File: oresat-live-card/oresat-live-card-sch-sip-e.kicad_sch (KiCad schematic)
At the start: 1 part, among them U7 OSD3358-512M-BSM

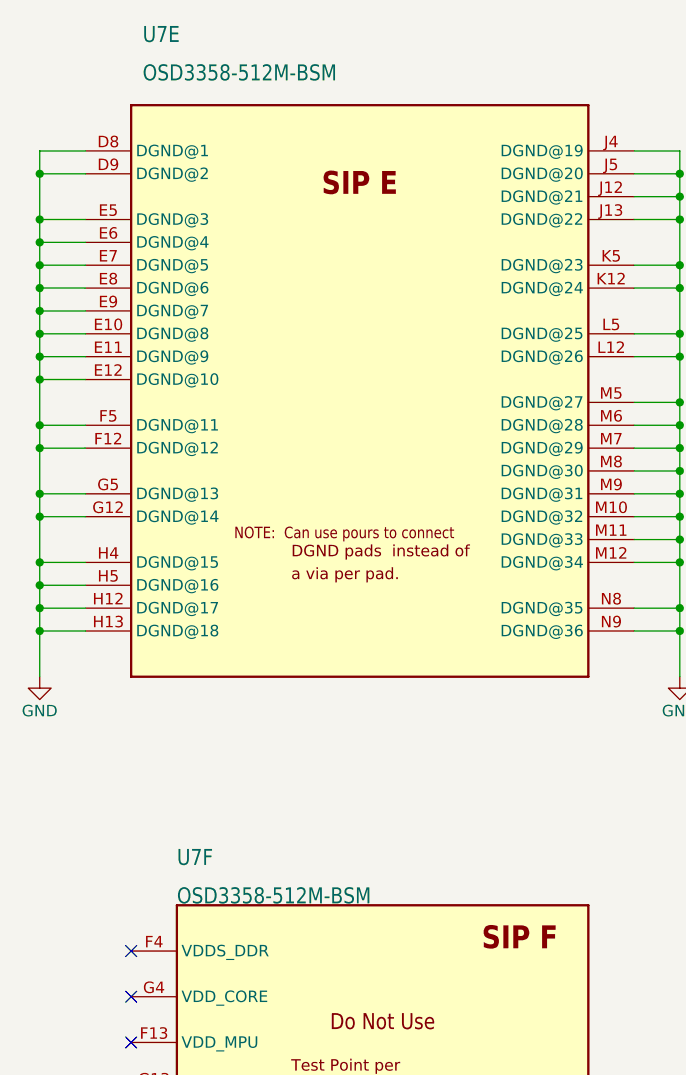
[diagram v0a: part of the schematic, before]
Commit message: BOM changes
Updated components outside of RF path to on hand parts.
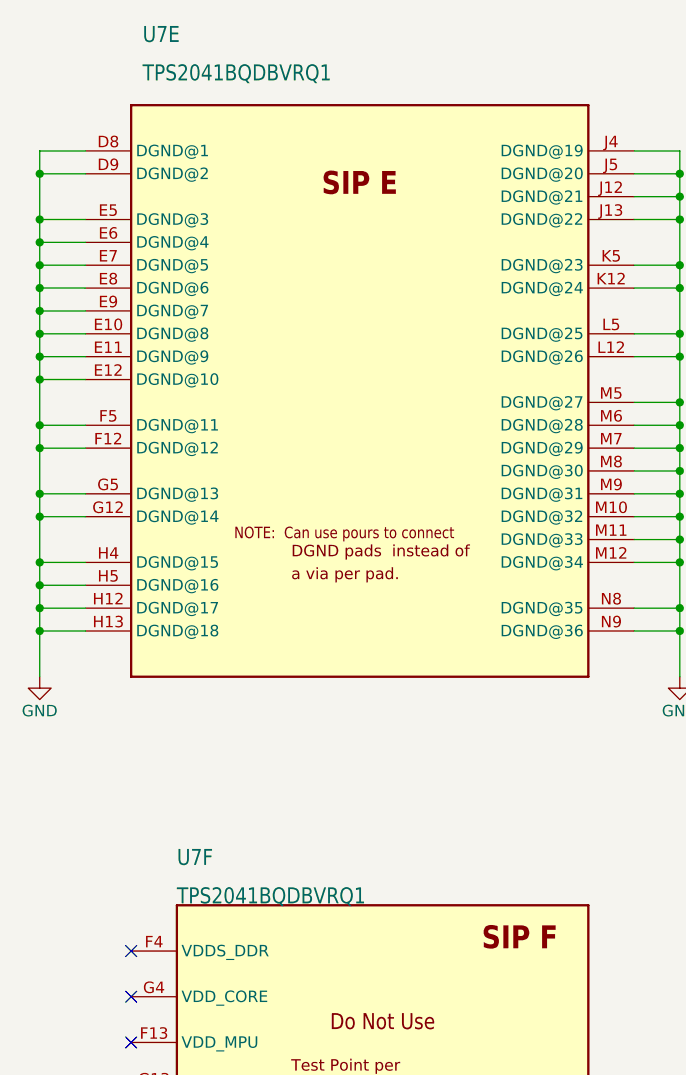
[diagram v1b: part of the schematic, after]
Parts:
- U7: value OSD3358-512M-BSM -> TPS2041BQDBVRQ1; footprint oresat-ics:U-Octavo-OSD335X-BGA-256 -> oresat-live-card:DBV5; DPN 1676-1002-ND -> 296-25159-1-ND; MFR Octavo Systems -> Texas Instruments; MPN OSD3358-512M-BSM -> TPS2041BQDBVRQ1
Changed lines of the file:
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@@
 			)
 		)
-		(property "Value" "OSD3358-512M-BSM"
+		(property "Value" "TPS2041BQDBVRQ1"
 			(at 162.56 52.07 0)
 			(show_name no)
@@
 			)
 		)
-		(property "Footprint" "oresat-ics:U-Octavo-OSD335X-BGA-256"
+		(property "Footprint" "oresat-live-card:DBV5"
 			(at 186.69 -22.86 0)
 			(hide yes)
@@
 			)
 		)
-		(property "Datasheet" ""
+		(property "Datasheet" "https://www.ti.com/lit/ds/symlink/tps2041b-q1.pdf?HQS=dis-dk-null-digikeymode-dsf-pf-null-wwe&ts=1651525711603&ref_url=https%253A%252F%252Fwww.ti.com%252Fgeneral%252Fdocs%252Fsuppproductinfo.tsp%253FdistId%253D10%2526gotoUrl%253Dhttps%253A%252F%252Fwww.ti.com%252Flit%252Fgpn%252Ftps2041b-q1"
 			(at 186.69 85.09 0)
 			(hide yes)
@@
 			)
 		)
-		(property "Description" "OSD335x Embedded Module 1GHz 512MB"
+		(property "Description" "Power Switch/Driver 1:1 N-Channel 500mA"
 			(at 186.69 85.09 0)
 			(hide yes)
@@
 			)
 		)
-		(property "MPN" "OSD3358-512M-BSM"
+		(property "MPN" "TPS2041BQDBVRQ1"
 			(at 186.69 85.09 0)
 			(hide yes)
@@
 			)
 		)
-		(property "DPN" "1676-1002-ND "
+		(property "DPN" "296-25159-1-ND "
 			(at 186.69 85.09 0)
 			(hide yes)
@@
 			)
 		)
-		(property "MFR" "Octavo Systems "
+		(property "MFR" "Texas Instruments "
 			(at 186.69 85.09 0)
 			(hide yes)
@@
 			)
 		)
-		(property "Value" "OSD3358-512M-BSM"
+		(property "Value" "TPS2041BQDBVRQ1"
 			(at 166.37 143.51 0)
 			(show_name no)
@@
 			)
 		)
-		(property "Footprint" "oresat-ics:U-Octavo-OSD335X-BGA-256"
+		(property "Footprint" "oresat-live-card:DBV5"
 			(at 189.23 60.96 0)
 			(hide yes)
@@
 			)
 		)
-		(property "Datasheet" ""
+		(property "Datasheet" "https://www.ti.com/lit/ds/symlink/tps2041b-q1.pdf?HQS=dis-dk-null-digikeymode-dsf-pf-null-wwe&ts=1651525711603&ref_url=https%253A%252F%252Fwww.ti.com%252Fgeneral%252Fdocs%252Fsuppproductinfo.tsp%253FdistId%253D10%2526gotoUrl%253Dhttps%253A%252F%252Fwww.ti.com%252Flit%252Fgpn%252Ftps2041b-q1"
 			(at 189.23 168.91 0)
 			(hide yes)
@@
 			)
 		)
-		(property "Description" "OSD335x Embedded Module 1GHz 512MB"
+		(property "Description" "Power Switch/Driver 1:1 N-Channel 500mA"
 			(at 189.23 168.91 0)
 			(hide yes)
@@
 			)
 		)
-		(property "MPN" "OSD3358-512M-BSM"
+		(property "MPN" "TPS2041BQDBVRQ1"
 			(at 189.23 168.91 0)
 			(hide yes)
@@
 			)
 		)
-		(property "DPN" "1676-1002-ND "
+		(property "DPN" "296-25159-1-ND "
 			(at 189.23 168.91 0)
 			(hide yes)
@@
 			)
 		)
-		(property "MFR" "Octavo Systems "
+		(property "MFR" "Texas Instruments "
 			(at 189.23 168.91 0)
 			(hide yes)

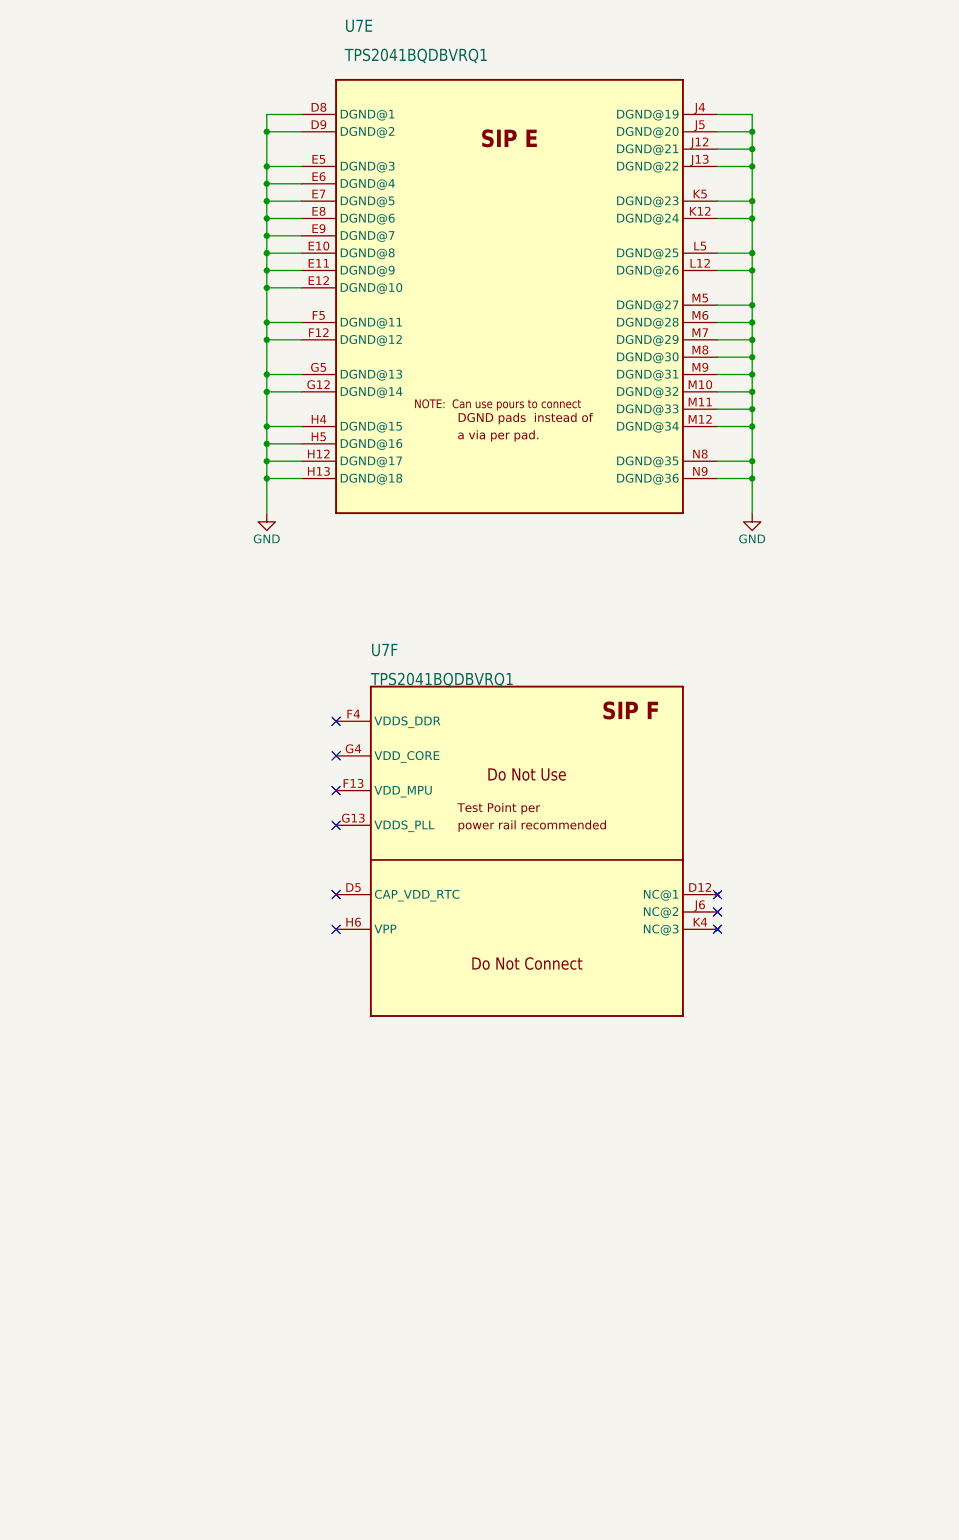
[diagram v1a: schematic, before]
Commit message: Cleanup of main sheet, no changes to functionality
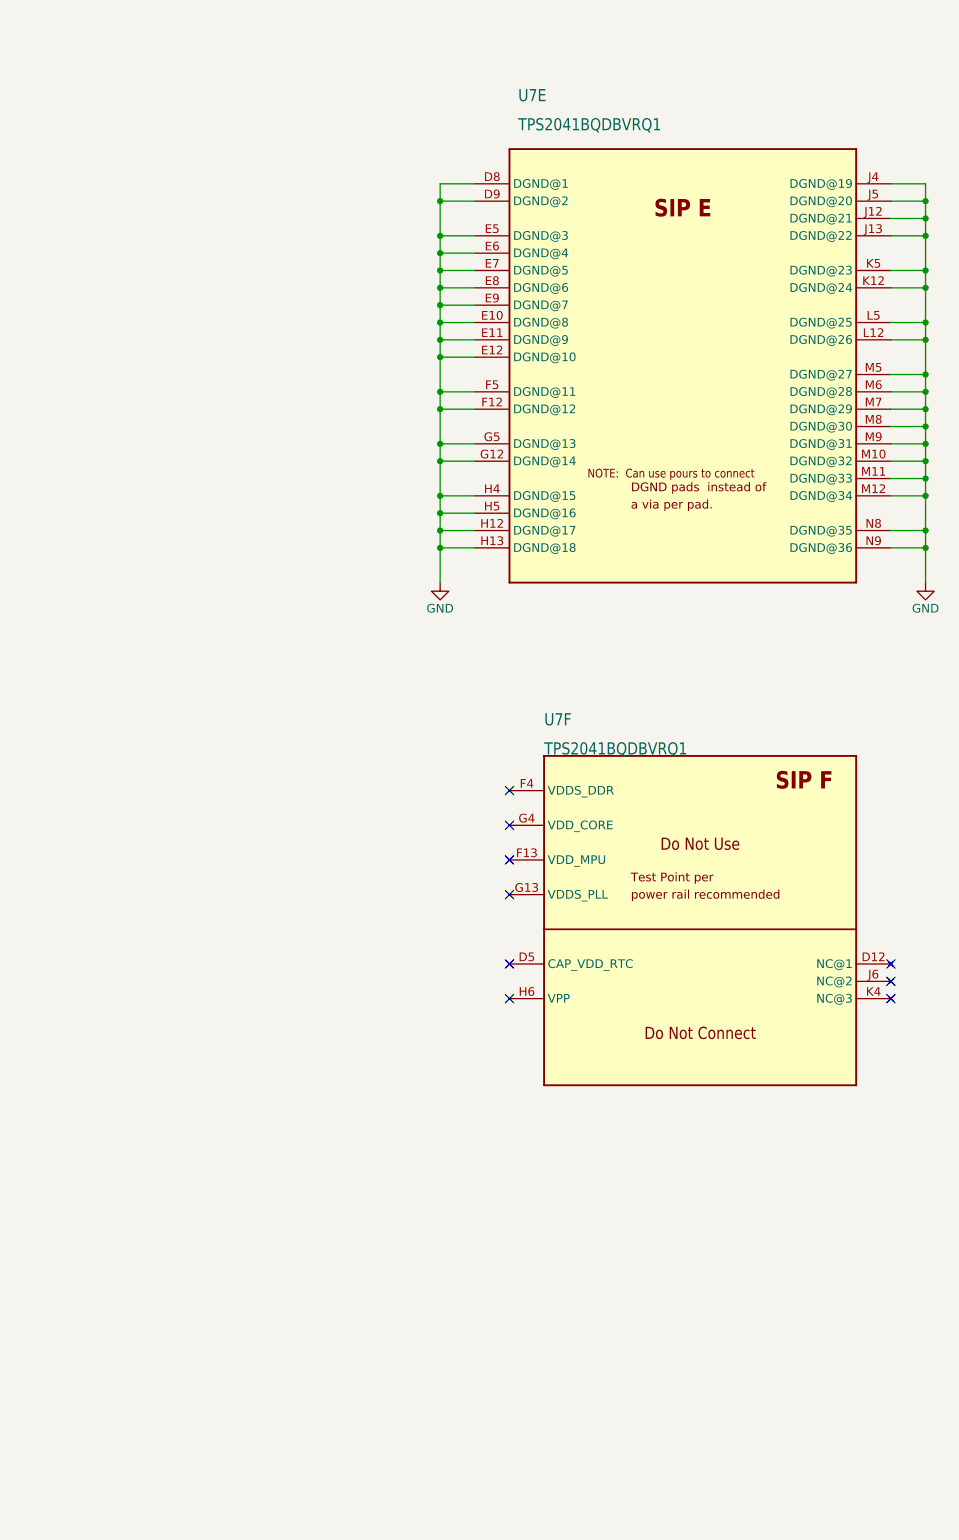
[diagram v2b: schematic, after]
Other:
- moved on the sheet: U7E, U7F

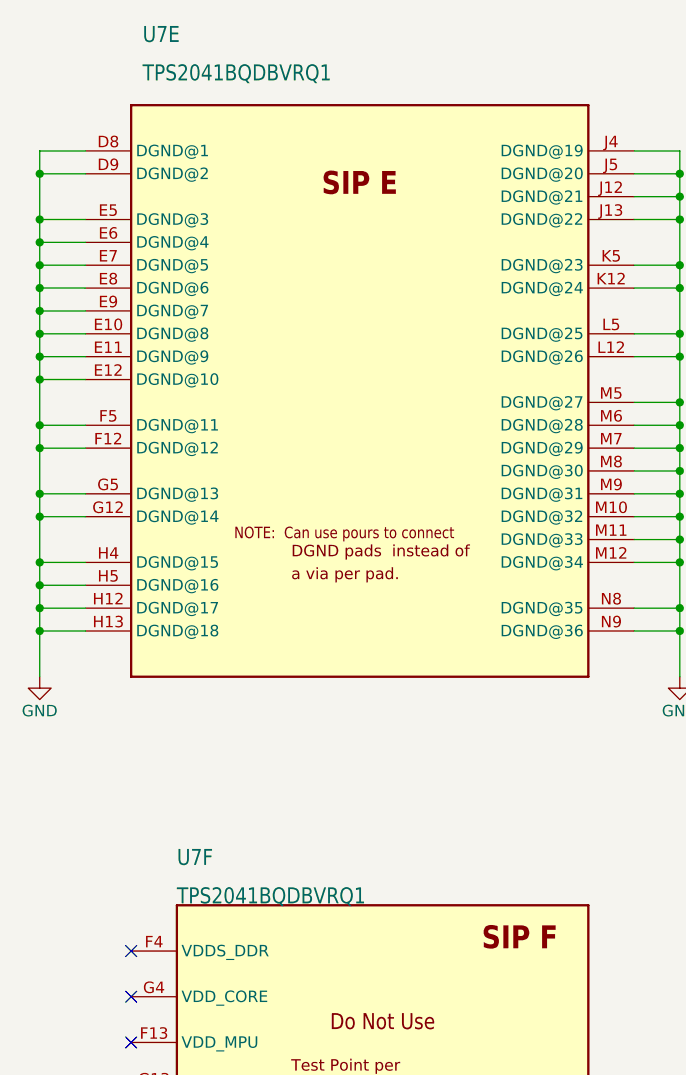
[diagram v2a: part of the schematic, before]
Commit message: BOM changed to match older version
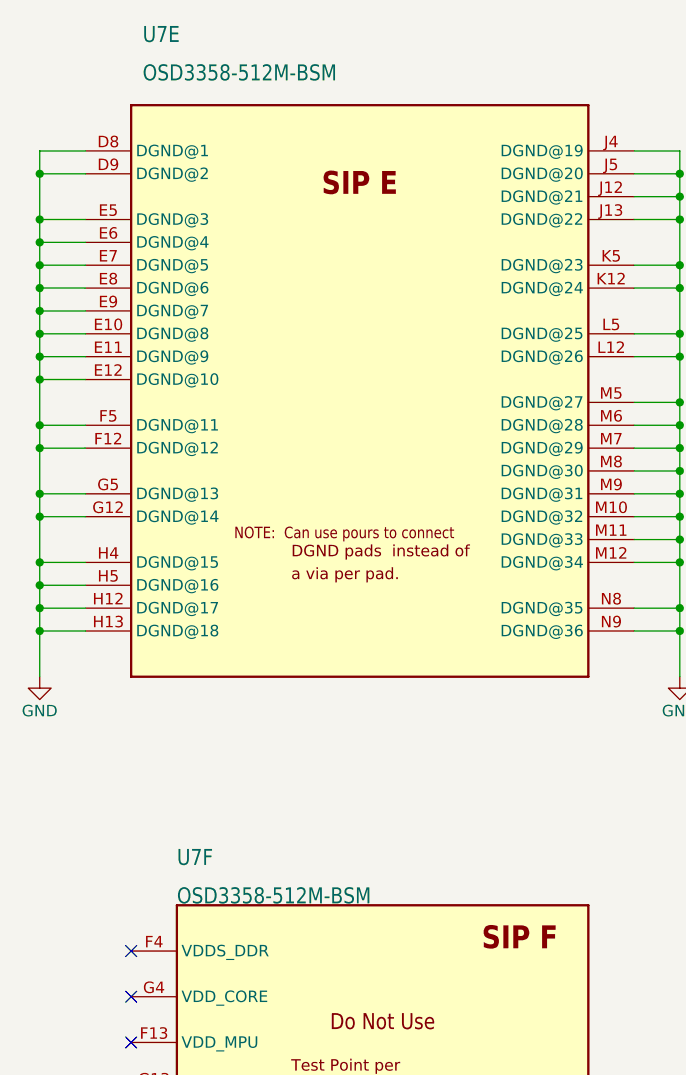
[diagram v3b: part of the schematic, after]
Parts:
- U7: value TPS2041BQDBVRQ1 -> OSD3358-512M-BSM; footprint oresat-live-card:DBV5 -> oresat-ics:U-Octavo-OSD335X-BGA-256; DPN 296-25159-1-ND -> 1676-1002-ND; MFR Texas Instruments -> Octavo Systems; MPN TPS2041BQDBVRQ1 -> OSD3358-512M-BSM
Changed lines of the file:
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@@
 			)
 		)
-		(property "Value" "TPS2041BQDBVRQ1"
+		(property "Value" "OSD3358-512M-BSM"
 			(at 187.96 62.23 0)
 			(show_name no)
@@
 			)
 		)
-		(property "Footprint" "oresat-live-card:DBV5"
+		(property "Footprint" "oresat-ics:U-Octavo-OSD335X-BGA-256"
 			(at 212.09 -12.7 0)
 			(hide yes)
@@
 			)
 		)
-		(property "Description" "Power Switch/Driver 1:1 N-Channel 500mA"
+		(property "Description" "OSD335x Embedded Module 1GHz 512MB"
 			(at 212.09 95.25 0)
 			(hide yes)
@@
 			)
 		)
-		(property "MPN" "TPS2041BQDBVRQ1"
+		(property "MPN" "OSD3358-512M-BSM"
 			(at 212.09 95.25 0)
 			(hide yes)
@@
 			)
 		)
-		(property "DPN" "296-25159-1-ND "
+		(property "DPN" "1676-1002-ND"
 			(at 212.09 95.25 0)
 			(hide yes)
@@
 			)
 		)
-		(property "MFR" "Texas Instruments "
+		(property "MFR" "Octavo Systems"
 			(at 212.09 95.25 0)
 			(hide yes)
@@
 			)
 		)
-		(property "Value" "TPS2041BQDBVRQ1"
+		(property "Value" "OSD3358-512M-BSM"
 			(at 191.77 153.67 0)
 			(show_name no)
@@
 			)
 		)
-		(property "Footprint" "oresat-live-card:DBV5"
+		(property "Footprint" "oresat-ics:U-Octavo-OSD335X-BGA-256"
 			(at 214.63 71.12 0)
 			(hide yes)
@@
 			)
 		)
-		(property "Description" "Power Switch/Driver 1:1 N-Channel 500mA"
+		(property "Description" "OSD335x Embedded Module 1GHz 512MB"
 			(at 214.63 179.07 0)
 			(hide yes)
@@
 			)
 		)
-		(property "MPN" "TPS2041BQDBVRQ1"
+		(property "MPN" "OSD3358-512M-BSM"
 			(at 214.63 179.07 0)
 			(hide yes)
@@
 			)
 		)
-		(property "DPN" "296-25159-1-ND "
+		(property "DPN" "1676-1002-ND"
 			(at 214.63 179.07 0)
 			(hide yes)
@@
 			)
 		)
-		(property "MFR" "Texas Instruments "
+		(property "MFR" "Octavo Systems"
 			(at 214.63 179.07 0)
 			(hide yes)

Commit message: mostly just polish after BOM fixes
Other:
- note added: "All resistors 0603 +/- 1% unless marked and AEQ certified unless otherwise marked. All caps are 0603 10% X5R or better and Vw >= 25 V and AEQ certified unless otherwise marked."
- moved on the sheet: U7F
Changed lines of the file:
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@@
 		(rev "2.1")
 	)
+	(text "All resistors 0603 +/- 1% unless marked and AEQ certified unless otherwise marked.\nAll caps are 0603 10% X5R or better and Vw >= 25 V and AEQ certified unless otherwise marked."
+		(exclude_from_sim no)
+		(at 114.046 265.938 0)
+		(effects
+			(font
+				(size 1.778 1.5113)
+			)
+			(justify left bottom)
+		)
+	)
 	(junction
 		(at 247.65 100.33)
@@
 	)
 	(no_connect
-		(at 186.69 163.83)
+		(at 185.42 163.83)
 	)
 	(no_connect
-		(at 242.57 189.23)
+		(at 241.3 189.23)
 	)
 	(no_connect
-		(at 242.57 186.69)
+		(at 241.3 186.69)
 	)
 	(no_connect
-		(at 186.69 189.23)
+		(at 185.42 189.23)
 	)
 	(no_connect
-		(at 242.57 184.15)
+		(at 241.3 184.15)
 	)
 	(no_connect
-		(at 186.69 168.91)
+		(at 185.42 168.91)
 	)
 	(no_connect
-		(at 186.69 184.15)
+		(at 185.42 184.15)
 	)
 	(no_connect
-		(at 186.69 173.99)
+		(at 185.42 173.99)
 	)
 	(no_connect
-		(at 186.69 158.75)
+		(at 185.42 158.75)
 	)
 	(wire
@@
 			(effects
 				(font
-					(size 1.778 1.5113)
+					(size 1.27 1.27)
 				)
 				(justify left top)
@@
 			(effects
 				(font
-					(size 1.778 1.5113)
+					(size 1.27 1.27)
 				)
 				(justify left bottom)
@@
 	(symbol
 		(lib_id "oresat-ics:OSD3358-512M-BSM")
-		(at 214.63 179.07 0)
+		(at 213.36 179.07 0)
 		(unit 6)
 		(body_style 1)
@@
 		(dnp no)
 		(property "Reference" "U7"
-			(at 191.77 147.32 0)
-			(show_name no)
-			(do_not_autoplace no)
-			(effects
-				(font
-					(size 1.778 1.5113)
+			(at 190.5 147.32 0)
+			(show_name no)
+			(do_not_autoplace no)
+			(effects
+				(font
+					(size 1.27 1.27)
 				)
 				(justify left top)
@@
 		)
 		(property "Value" "OSD3358-512M-BSM"
-			(at 191.77 153.67 0)
-			(show_name no)
-			(do_not_autoplace no)
-			(effects
-				(font
-					(size 1.778 1.5113)
+			(at 190.5 153.67 0)
+			(show_name no)
+			(do_not_autoplace no)
+			(effects
+				(font
+					(size 1.27 1.27)
 				)
 				(justify left bottom)
@@
 		)
 		(property "Footprint" "oresat-ics:U-Octavo-OSD335X-BGA-256"
-			(at 214.63 71.12 0)
+			(at 213.36 71.12 0)
 			(hide yes)
 			(show_name no)
@@
 		)
 		(property "Datasheet" "https://www.ti.com/lit/ds/symlink/tps2041b-q1.pdf?HQS=dis-dk-null-digikeymode-dsf-pf-null-wwe&ts=1651525711603&ref_url=https%253A%252F%252Fwww.ti.com%252Fgeneral%252Fdocs%252Fsuppproductinfo.tsp%253FdistId%253D10%2526gotoUrl%253Dhttps%253A%252F%252Fwww.ti.com%252Flit%252Fgpn%252Ftps2041b-q1"
-			(at 214.63 179.07 0)
+			(at 213.36 179.07 0)
 			(hide yes)
 			(show_name no)
@@
 		)
 		(property "Description" "OSD335x Embedded Module 1GHz 512MB"
-			(at 214.63 179.07 0)
+			(at 213.36 179.07 0)
 			(hide yes)
 			(show_name no)
@@
 		)
 		(property "MPN" "OSD3358-512M-BSM"
-			(at 214.63 179.07 0)
+			(at 213.36 179.07 0)
 			(hide yes)
 			(show_name no)
@@
 		)
 		(property "DPN" "1676-1002-ND"
-			(at 214.63 179.07 0)
+			(at 213.36 179.07 0)
 			(hide yes)
 			(show_name no)
@@
 		)
 		(property "MFR" "Octavo Systems"
-			(at 214.63 179.07 0)
+			(at 213.36 179.07 0)
 			(hide yes)
 			(show_name no)
@@
 		)
 		(property "DIS" "DigiKey"
-			(at 214.63 179.07 0)
-			(hide yes)
-			(show_name no)
+			(at 213.36 179.07 0)
+			(hide yes)
+			(show_name no)
